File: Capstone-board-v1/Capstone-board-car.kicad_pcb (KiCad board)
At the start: 2 copper layers, 25 parts, among them J1 Pcio Socket 1, J2 Pico Socket 2, J3 Ultra Sonic Sensor, J4 Car, J5 Camera, U1 3.3V Voltage Regulator, U2 555 Timer, U3 5V Voltage Regulator 2, U4 5V Voltage Regulator 1

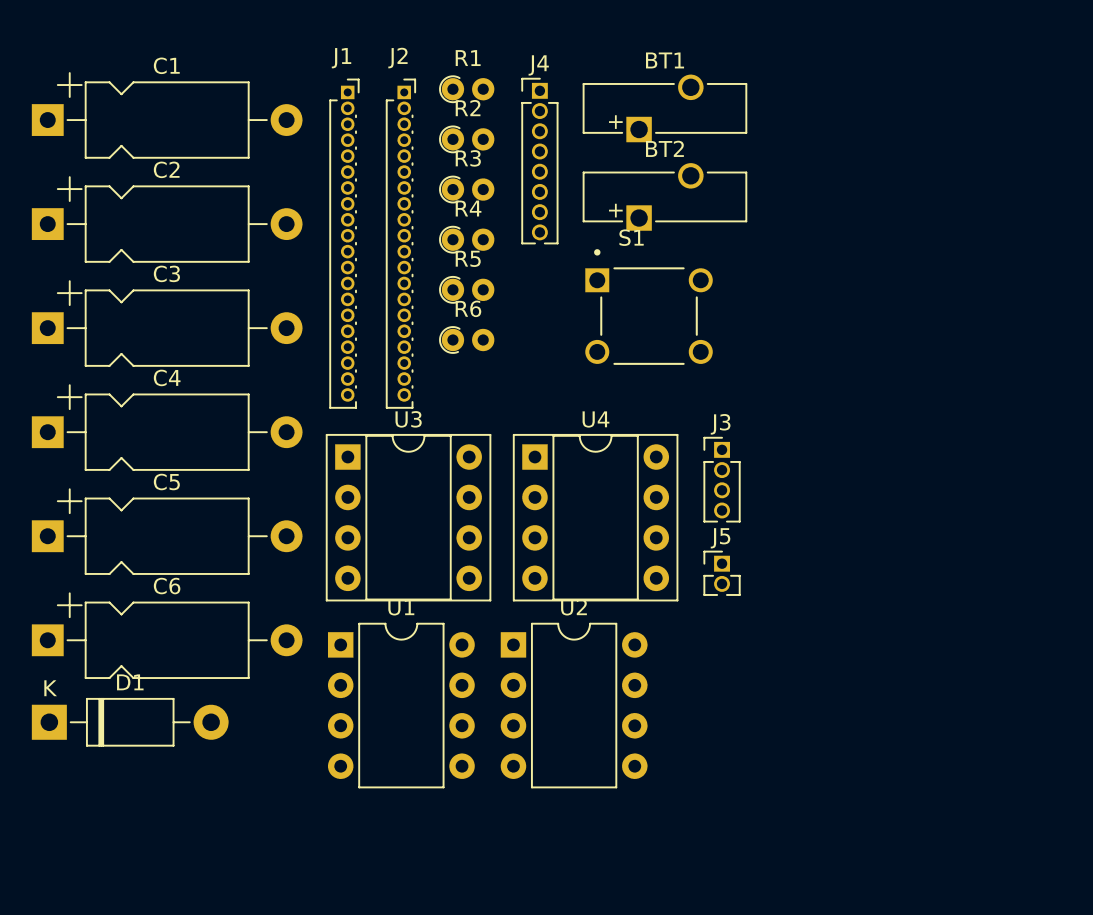
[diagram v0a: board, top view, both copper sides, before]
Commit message: correct hole size
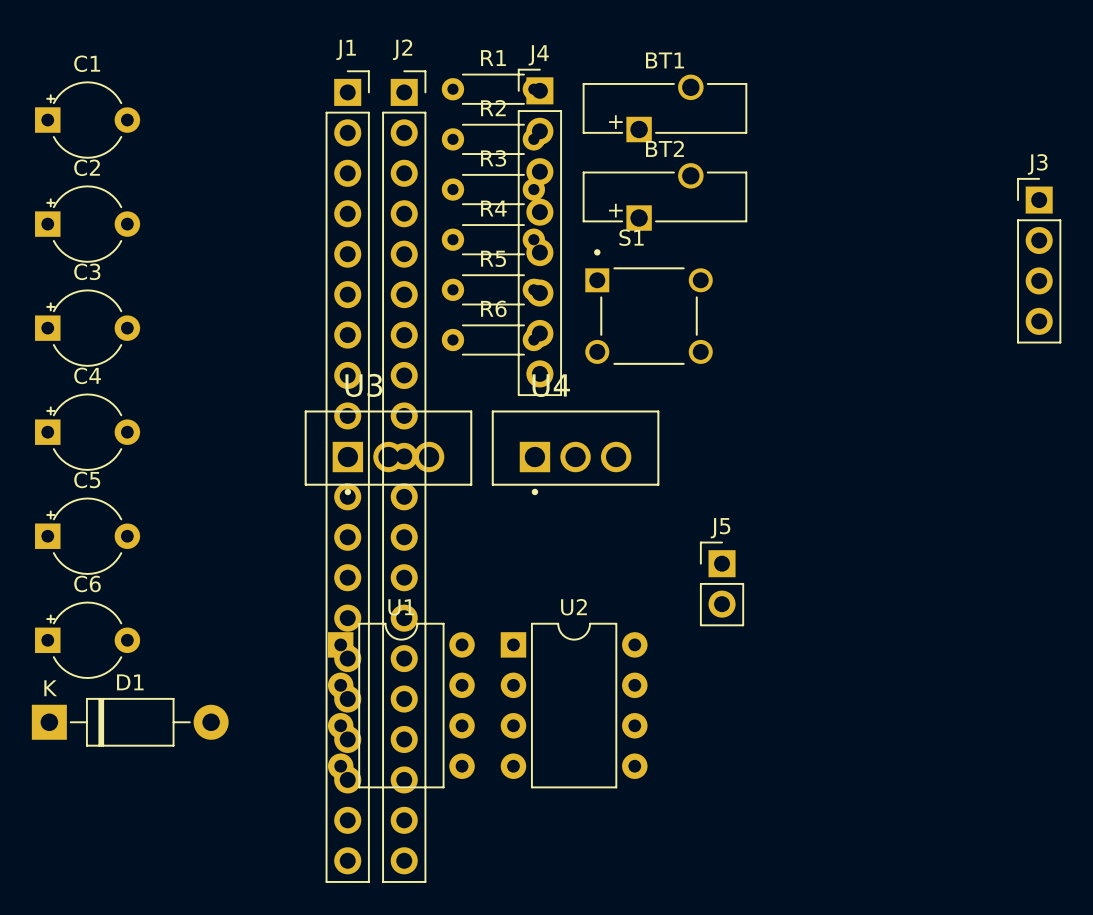
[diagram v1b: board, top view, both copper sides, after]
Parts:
- C1, C2, C3, C4, C5, C6: footprint Capacitor_THT:CP_Axial_L10.0mm_D4.5mm_P15.00mm_Horizontal -> Capacitor_THT:CP_Radial_Tantal_D4.5mm_P5.00mm
- J1, J2: footprint Connector_PinSocket_1.00mm:PinSocket_1x20_P1.00mm_Vertical -> Connector_PinSocket_2.54mm:PinSocket_1x20_P2.54mm_Vertical
- J3: footprint Connector_PinHeader_1.27mm:PinHeader_1x04_P1.27mm_Vertical -> Connector_PinHeader_2.54mm:PinHeader_1x04_P2.54mm_Vertical
- J4: footprint Connector_PinHeader_1.27mm:PinHeader_1x08_P1.27mm_Vertical -> Connector_PinHeader_2.54mm:PinHeader_1x08_P2.54mm_Vertical
- J5: footprint Connector_PinHeader_1.27mm:PinHeader_1x02_P1.27mm_Vertical -> Connector_PinHeader_2.54mm:PinHeader_1x02_P2.54mm_Vertical
- R1, R2, R3, R4, R5, R6: footprint Resistor_THT:R_Axial_DIN0204_L3.6mm_D1.6mm_P1.90mm_Vertical -> Resistor_THT:R_Axial_DIN0204_L3.6mm_D1.6mm_P5.08mm_Horizontal
- U3, U4: footprint Package_DIP:DIP-8_W7.62mm_Socket -> LinReg:TO255P1040X460X1968-3
- moved J3 25.4 mm to (172.7, 53.3)

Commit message: traces added
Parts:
- added J6: Gyroscope Sensor, Connector_PinSocket_2.54mm:PinSocket_1x08_P2.54mm_Vertical, F.Cu at (59.9, 78.7)
- BT1: footprint Battery:Battery_Panasonic_CR1025-VSK_Vertical_CircularHoles -> Connector_Hirose:Hirose_DF11-4DP-2DSA_2x02_P2.00mm_Vertical
- BT2: footprint Battery:Battery_Panasonic_CR1025-VSK_Vertical_CircularHoles -> Connector_PinHeader_2.54mm:PinHeader_1x02_P2.54mm_Vertical
- R4: value 270Ohms -> 10Ohms
- S1: footprint TS02-66-60-BK-100-LCR-D:SW_TS02-66-60-BK-160-LCR-D -> TS:SW_TS02-66-60-BK-160-LCR-D
- moved S1 121.6 mm to (41.9, 119.6)
- moved BT1 114.4 mm to (56.9, 118.6)
- moved R1 114.3 mm to (47.8, 119.1)
- moved R3 111.9 mm to (47.8, 121.7)
- moved R2 110.8 mm to (47.8, 116.6)
- moved J3 110.1 mm to (65.5, 78.7), turned to 90 degrees
- moved J2 103.6 mm to (41.7, 95.7), turned to 90 degrees
- moved BT2 99.8 mm to (72.9, 120.7), turned to 90 degrees
- moved J5 97.9 mm to (65.5, 120.7), turned to 90 degrees
- moved C1 95.8 mm to (38.9, 112.0)
- moved R5 92.8 mm to (63.5, 117.1)
- moved R6 84.4 mm to (71.9, 117.1)
- moved U4 78.8 mm to (81.3, 120.9)
- moved C6 77.4 mm to (44.2, 40.9)
- moved C5 77.3 mm to (38.6, 103.1)
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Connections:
- J2 pad 1: unconnected-(J2-Pin_1-Pad1) -> Net-(J2-Pin_1)
- J2 pad 2: unconnected-(J2-Pin_2-Pad2) -> Net-(J2-Pin_2)

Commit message: All routing done.
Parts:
- moved C2 83.9 mm to (46.3, 103.1)
- moved C6 63.1 mm to (54.7, 103.1)
- moved U3 53.9 mm to (86.1, 114.6), turned to 180 degrees
- moved J4 45.5 mm to (81.8, 99.6)
- moved R4 29.2 mm to (73.9, 117.6), turned to 90 degrees
- moved D1 13.7 mm to (87.4, 99.8), turned to -90 degrees
- moved J6 10.9 mm to (69.8, 74.2), turned to 90 degrees
- moved J3 8.45 mm to (58.4, 74.2)
- moved R6 7.15 mm to (73.9, 110.2), turned to 90 degrees
- moved J1 6.82 mm to (87.6, 78.0)
- moved U1 3.78 mm to (76.7, 103.1)
- moved BT1 2.34 mm to (59.2, 118.1), turned to -90 degrees
- moved J2 2.30 mm to (39.4, 95.8)
- moved J5 1.04 mm to (64.5, 120.9)
- moved C1 0.51 mm to (38.4, 112.0)
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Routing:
- net Earth: track 0.00 -> 178.5 mm
- net Net-(J3-Pin_1): track 0.00 -> 79.6 mm
- net VCCQ: track 0.00 -> 76.6 mm
- net Net-(J2-Pin_19): track 0.00 -> 76.2 mm
- net Net-(J2-Pin_2): track 0.00 -> 65.1 mm
- net VCC: track 0.00 -> 58.1 mm
- net Net-(J5-Pin_1): track 0.00 -> 53.3 mm
- net Net-(J2-Pin_1): track 0.00 -> 50.4 mm
- net Net-(D1-A): track 0.00 -> 43.7 mm
- net Net-(U2-THR): track 0.00 -> 32.7 mm
- net Net-(J1-Pin_2): track 0.00 -> 26.8 mm
- net Net-(J1-Pin_1): track 0.00 -> 26.8 mm
- net Net-(J1-Pin_6): track 0.00 -> 25.1 mm
- net Net-(J1-Pin_4): track 0.00 -> 25.1 mm
- net Net-(J1-Pin_7): track 0.00 -> 25.1 mm
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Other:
- board outline added: 53.6 x 52.8 mm

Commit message: Some footprints fixed.
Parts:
- U1, U2: footprint Package_DIP:DIP-8_W7.62mm -> Package_DIP:DIP-8_W7.62mm_Socket
- moved D1 0.25 mm to (87.6, 99.8)
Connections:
- J6 pad 3: Net-(J2-Pin_1) -> Net-(J2-Pin_2)
- J6 pad 4: Net-(J2-Pin_2) -> Net-(J2-Pin_1)
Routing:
- net Net-(J2-Pin_2): track 65.1 -> 47.3 mm
- net Net-(J2-Pin_1): track 50.4 -> 52.9 mm

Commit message: Final traces done
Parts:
- moved D1 0.36 mm to (87.9, 100.1)
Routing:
- net VCC: track 58.1 -> 73.4 mm
- net VCCQ: track 76.6 -> 87.4 mm
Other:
- board size 53.6 x 52.8 mm -> 54.1 x 52.8 mm

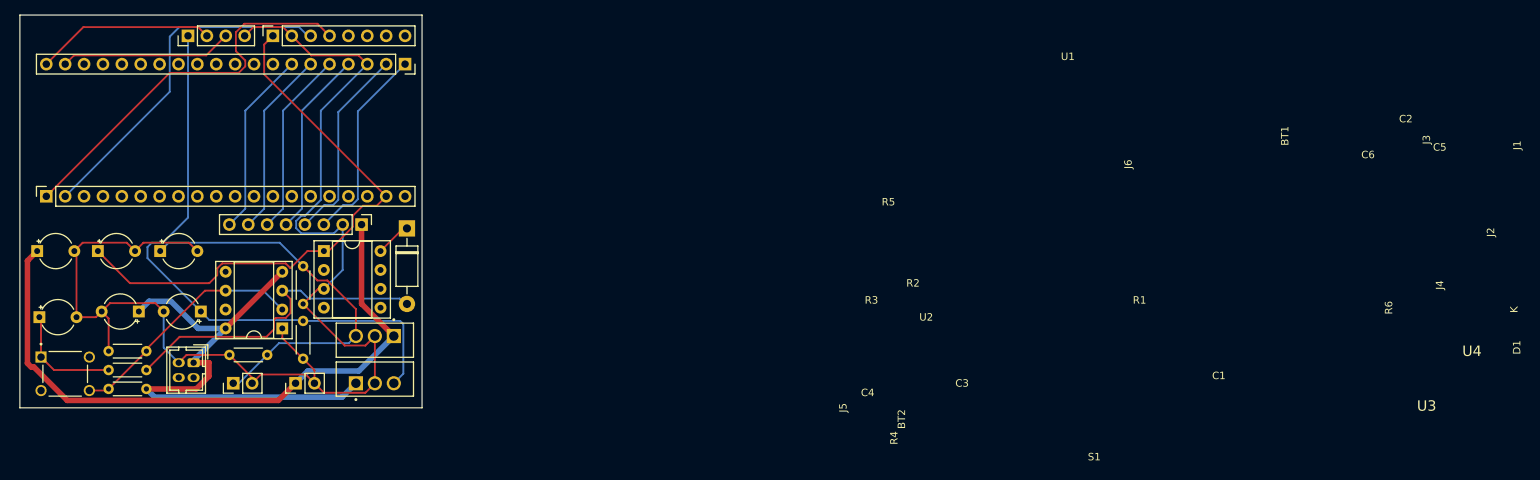
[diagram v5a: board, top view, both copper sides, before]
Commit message: reference designators added
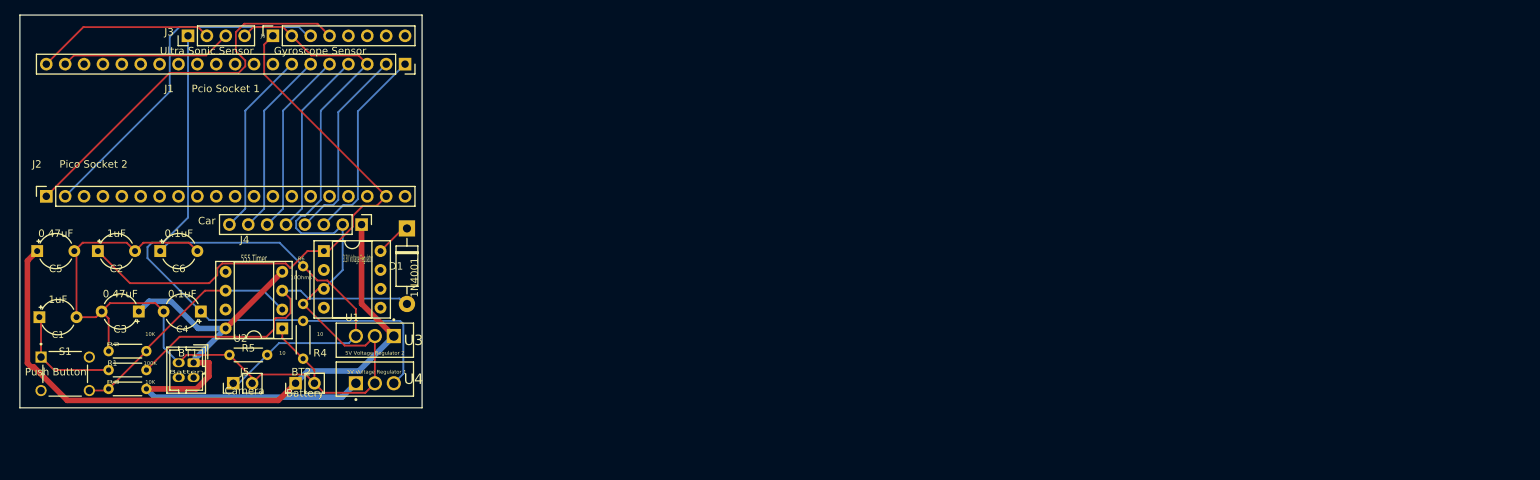
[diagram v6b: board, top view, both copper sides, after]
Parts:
- R1: value 100KOhms -> 100K
- R2, R3: value 10KOhms -> 10K
- R4, R5: value 10Ohms -> 10

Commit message: Final PCB completed!
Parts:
- removed D1: 1N4001, Diode_THT:D_DO-41_SOD81_P10.16mm_Horizontal
- J1: value Pcio Socket 1 -> Pico Socket 1
- R1: value 100K -> 100KOhms
- R2, R3: value 10K -> 10KOhms
- R4, R5: value 10 -> 10Ohms
- U1: value 3.3V Voltage Regulator -> 3.3V V.R
- U3: value 5V Voltage Regulator 2 -> 5V V.R 2
- U4: value 5V Voltage Regulator 1 -> 5V V.R 1
- moved U1 2.30 mm to (79.0, 103.2)
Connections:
- R1 pad 2: Net-(D1-A) -> Net-(U1-IN)
- U1 pad 8: Net-(D1-K) -> Net-(U1-IN)
- U2 pad 3: Net-(D1-A) -> Net-(U1-IN)
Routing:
- net Net-(U1-IN): track 0.00 -> 47.7 mm
- net Net-(D1-A): track 43.7 -> 0.00 mm
- net Earth: track 178.5 -> 191.6 mm
- net Net-(D1-K): track 4.56 -> 0.00 mm
- net Net-(J2-Pin_1): track 52.9 -> 54.7 mm
- net VCC: track 73.4 -> 74.5 mm
- net Net-(J2-Pin_19): track 76.2 -> 77.1 mm
- net Net-(J3-Pin_1): track 79.6 -> 80.5 mm
- net Net-(J1-Pin_1): track 26.8 -> 27.4 mm
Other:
- board size 54.1 x 52.8 mm -> 54 x 53.3 mm

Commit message: Final PCB's done.
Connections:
- C3 pad 1: VCC -> Net-(U1-IN)
- U4 pad 1: VCC -> Net-(U1-IN)
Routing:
- net VCC: track 74.5 -> 31.2 mm
- net Net-(U1-IN): track 47.7 -> 82.8 mm
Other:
- board size 54 x 53.3 mm -> 54.3 x 54.3 mm
- board text added: "Capstone Fall 2023: Epitome | Team Members: Ruhul Quddus, Goutham Mittadhoddi, Nima Razavi, Ian Le, Kenny Zhang"
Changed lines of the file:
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@@
     (pad_to_mask_clearance 0)
     (pcbplotparams
-      (layerselection 0x00010fc_ffffffff)
+      (layerselection 0x00010f0_ffffffff)
       (plot_on_all_layers_selection 0x0000000_00000000)
       (disableapertmacros false)
@@
       (outputformat 1)
       (mirror false)
-      (drillshape 1)
+      (drillshape 0)
       (scaleselection 1)
-      (outputdirectory "")
+      (outputdirectory "C:/Users/ruhul/OneDrive/Desktop/Capstone/capstone-project/Car PCB Gerber Files/")
     )
   )
@@
     (property "ki_keywords" "LT1121CN8#PBF")
     (attr through_hole)
-    (fp_text reference "U1" (at -2.148 -0.554) (layer "F.SilkS")
-        (effects (font (size 0.5 0.5) (thickness 0.125)))
-    )
-    (fp_text value "3.3V V.R" (at -3.258 -1.264) (layer "F.SilkS")
+    (fp_text reference "U1" (at -2.52 -0.51) (layer "F.SilkS")
+        (effects (font (size 0.5 0.5) (thickness 0.125)))
+    )
+    (fp_text value "3.3V V.R" (at -3.5 -1.31) (layer "F.SilkS")
         (effects (font (size 0.5 0.5) (thickness 0.125)))
     )
@@
     (fp_line (start 4 3.5) (end 4 -1.5)
       (stroke (width 0.1) (type solid)) (layer "F.Fab"))
-    (pad "1" thru_hole roundrect (at 0 0 270) (size 1.2 1.65) (drill 0.85) (layers "*.Cu" "*.Mask") (roundrect_rratio 0.208333)
+    (pad "1" thru_hole roundrect (at 0 0 270) (size 1.2 1.65) (drill 0.85) (layers "*.Cu" "*.Mask") (roundrect_rratio 0.2083333333)
       (net 1 "VCC") (pinfunction "+") (pintype "passive"))
     (pad "2" thru_hole oval (at 0 2 270) (size 1.2 1.65) (drill 0.85) (layers "*.Cu" "*.Mask")
@@
     (property "ki_keywords" "Voltage Regulator 1.5A Positive")
     (attr through_hole)
-    (fp_text reference "U4" (at 1.204 2.536) (layer "F.SilkS")
-        (effects (font (size 0.5 0.5) (thickness 0.125)))
-    )
-    (fp_text value "5V V.R 1" (at 3.584 2.516) (layer "F.SilkS")
+    (fp_text reference "U4" (at -2.556 2.566) (layer "F.SilkS")
+        (effects (font (size 0.5 0.5) (thickness 0.125)))
+    )
+    (fp_text value "5V V.R 1" (at -0.036 2.856) (layer "F.SilkS")
         (effects (font (size 0.5 0.5) (thickness 0.125)))
     )
@@
       (stroke (width 0.2) (type solid)) (fill none) (layer "F.Fab"))
     (pad "1" thru_hole rect (at 0 0) (size 1.91 1.91) (drill 1.27) (layers "*.Cu" "*.Mask")
-      (net 1 "VCC") (pinfunction "IN") (pintype "power_in") (solder_mask_margin 0.102))
+      (net 8 "Net-(U1-IN)") (pinfunction "IN") (pintype "power_in") (solder_mask_margin 0.102))
     (pad "2" thru_hole circle (at 2.55 0) (size 1.91 1.91) (drill 1.27) (layers "*.Cu" "*.Mask")
       (net 2 "Earth") (pinfunction "GND") (pintype "power_in") (solder_mask_margin 0.102))
@@
     (property "ki_keywords" "connector")
     (attr through_hole)
-    (fp_text reference "J2" (at 2.218 49.53 180) (layer "F.SilkS")
-        (effects (font (size 0.5 0.5) (thickness 0.125)))
-    )
-    (fp_text value "Pico Socket 2" (at 2.228 46.18 180) (layer "F.SilkS")
+    (fp_text reference "J2" (at 3.058 47.46 180) (layer "F.SilkS")
+        (effects (font (size 0.5 0.5) (thickness 0.125)))
+    )
+    (fp_text value "Pico Socket 2" (at 2.278 47.29 180) (layer "F.SilkS")
         (effects (font (size 0.5 0.5) (thickness 0.125)))
     )
@@
         (effects (font (size 0.5 0.5) (thickness 0.125)))
     )
-    (fp_text value "Gyroscope Sensor" (at 2.288 10.56 180) (layer "F.SilkS")
-        (effects (font (size 0.5 0.5) (thickness 0.125)))
-    )
-    (fp_text user "${REFERENCE}" (at 2.238 6.54) (layer "F.SilkS")
+    (fp_text value "Gyroscope Sensor" (at 2.308 16.52 180) (layer "F.SilkS")
+        (effects (font (size 0.5 0.5) (thickness 0.125)))
+    )
+    (fp_text user "${REFERENCE}" (at 2.958 16.86) (layer "F.SilkS")
         (effects (font (size 0.5 0.5) (thickness 0.125)))
     )
@@
       (stroke (width 0.1) (type solid)) (fill none) (layer "F.Fab"))
     (pad "1" thru_hole rect (at 0 0 180) (size 1.6 1.6) (drill 0.8) (layers "*.Cu" "*.Mask")
-      (net 1 "VCC") (pintype "passive"))
+      (net 8 "Net-(U1-IN)") (pintype "passive"))
     (pad "2" thru_hole circle (at 5 0 180) (size 1.6 1.6) (drill 0.8) (layers "*.Cu" "*.Mask")
       (net 2 "Earth") (pintype "passive"))
@@
     )
   )
-  (gr_rect (start 35.724 71.264) (end 89.746 124.606)
+  (gr_rect (start 35.724 70.444) (end 90.066 124.776)
     (stroke (width 0.05) (type default)) (fill none) (layer "Edge.Cuts"))
+  (gr_text "Capstone Fall 2023: Epitome | Team Members: Ruhul Quddus, Goutham Mittadhoddi, Nima Razavi, Ian Le, Kenny Zhang\n" (at 59.2 71.25) (layer "F.SilkS")
+    (effects (font (size 0.5 0.5) (thickness 0.125)))
+  )
+  (dimension (type aligned) (layer "B.Cu")
+    (pts (xy 90.066 124.776) (xy 90.066 70.444))
+    (height 14.134)
+    (gr_text "54.3320 mm" (at 102.4 97.61 90) (layer "B.Cu")
+      (effects (font (size 1.5 1.5) (thickness 0.3)))
+    )
+    (format (prefix "") (suffix "") (units 3) (units_format 1) (precision 4))
+    (style (thickness 0.2) (arrow_length 1.27) (text_position_mode 0) (extension_height 0.58642) (extension_offset 0.5) keep_text_aligned)
+  )
+  (dimension (type aligned) (layer "B.Cu")
+    (pts (xy 35.724 124.776) (xy 90.066 124.776))
+    (height 5.034)
+    (gr_text "54.3420 mm" (at 62.895 128.01) (layer "B.Cu")
+      (effects (font (size 1.5 1.5) (thickness 0.3)))
+    )
+    (format (prefix "") (suffix "") (units 3) (units_format 1) (precision 4))
+    (style (thickness 0.2) (arrow_length 1.27) (text_position_mode 0) (extension_height 0.58642) (extension_offset 0.5) keep_text_aligned)
+  )
   (segment (start 59.182 118.142) (end 61.246 118.142) (width 0.75) (layer "F.Cu") (net 1))
   (segment (start 63.49 113.21) (end 63.49 113.528) (width 0.75) (layer "F.Cu") (net 1))
@@
   (segment (start 60.684 117.836) (end 63.49 115.03) (width 0.75) (layer "B.Cu") (net 1))
   (segment (start 63.49 115.03) (end 63.49 113.528) (width 0.75) (layer "B.Cu") (net 1))
-  (segment (start 53.338 109.73) (end 55.991 109.73) (width 0.75) (layer "B.Cu") (net 1))
-  (segment (start 59.789 113.528) (end 63.49 113.528) (width 0.75) (layer "B.Cu") (net 1))
-  (segment (start 55.991 109.73) (end 59.789 113.528) (width 0.75) (layer "B.Cu") (net 1))
-  (segment (start 79.141 122.779) (end 53.945 122.779) (width 0.75) (layer "B.Cu") (net 1))
-  (segment (start 53.945 122.779) (end 52.832 121.666) (width 0.75) (layer "B.Cu") (net 1))
-  (segment (start 51.816 111.252) (end 53.338 109.73) (width 0.75) (layer "B.Cu") (net 1))
-  (segment (start 81.016 120.904) (end 79.141 122.779) (width 0.75) (layer "B.Cu") (net 1))
   (segment (start 59.182 118.142) (end 59.182 117.836) (width 0.25) (layer "B.Cu") (net 1))
   (segment (start 64.008 117.094) (end 67.056 120.142) (width 0.25) (layer "F.Cu") (net 2))
@@
   (segment (start 52.832 119.126) (end 53.166 119.46) (width 0.25) (layer "F.Cu") (net 8))
   (segment (start 56.638 115.32) (end 52.832 119.126) (width 0.75) (layer "F.Cu") (net 8))
+  (segment (start 88.65 112.46) (end 82.2 112.46) (width 0.75) (layer "B.Cu") (net 8))
+  (segment (start 54.458 116.407949) (end 54.47 116.419949) (width 0.75) (layer "B.Cu") (net 8))
+  (segment (start 88.64 112.47) (end 88.65 112.46) (width 0.75) (layer "B.Cu") (net 8))
+  (segment (start 81.016 120.904) (end 83.072 122.96) (width 0.75) (layer "B.Cu") (net 8))
   (segment (start 78.28 112.47) (end 74.258 108.448) (width 0.75) (layer "B.Cu") (net 8))
+  (segment (start 88.64 122.96) (end 88.64 112.47) (width 0.75) (layer "B.Cu") (net 8))
+  (segment (start 82.2 112.46) (end 82.19 112.47) (width 0.75) (layer "B.Cu") (net 8))
+  (segment (start 83.072 122.96) (end 88.64 122.96) (width 0.75) (layer "B.Cu") (net 8))
   (segment (start 82.19 107.59) (end 82.19 112.47) (width 0.75) (layer "B.Cu") (net 8))
   (segment (start 86.63 103.15) (end 82.19 107.59) (width 0.75) (layer "B.Cu") (net 8))
+  (segment (start 54.47 117.488) (end 52.832 119.126) (width 0.75) (layer "B.Cu") (net 8))
+  (segment (start 51.816 111.252) (end 54.458 113.894) (width 0.75) (layer "B.Cu") (net 8))
   (segment (start 71.11 109.08) (end 71.11 108.448) (width 0.25) (layer "B.Cu") (net 8))
   (segment (start 82.19 112.47) (end 78.28 112.47) (width 0.75) (layer "B.Cu") (net 8))
   (segment (start 74.258 108.448) (end 71.11 108.448) (width 0.75) (layer "B.Cu") (net 8))
+  (segment (start 54.47 116.419949) (end 54.47 117.488) (width 0.75) (layer "B.Cu") (net 8))
+  (segment (start 54.458 113.894) (end 54.458 116.407949) (width 0.75) (layer "B.Cu") (net 8))
   (segment (start 79.126 97.13) (end 81.28 97.13) (width 0.25) (layer "B.Cu") (net 9))
   (segment (start 76.698 99.558) (end 79.126 97.13) (width 0.25) (layer "B.Cu") (net 9))
